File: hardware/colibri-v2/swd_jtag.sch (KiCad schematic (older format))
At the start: 9 parts

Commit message: ADDED R1, R2 R3
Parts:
- added R1, R2, R3: 10K, Resistors_SMD:R_0603, symbol R
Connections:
- net +3V3: now also R1.2, R2.2, R3.2
- net TCK/SWCLK: now also R1.1
- net TDO/SWO: now also R3.1
- net TMS/SWDIO: now also R2.1
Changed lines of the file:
@@
 	1    0    0    -1
 $EndComp
-Wire Wire Line
-	3500 2000 3300 2000
-Wire Wire Line
-	3300 2000 3300 3350
-Wire Wire Line
-	3500 2100 3300 2100
-Connection ~ 3300 2100
-Wire Wire Line
-	3500 2200 3300 2200
-Connection ~ 3300 2200
-Wire Wire Line
-	3500 2300 3300 2300
-Connection ~ 3300 2300
-Wire Wire Line
-	3500 2400 3300 2400
-Connection ~ 3300 2400
-Wire Wire Line
-	3500 2500 3300 2500
-Connection ~ 3300 2500
-Wire Wire Line
-	3500 2600 3300 2600
-Connection ~ 3300 2600
-Wire Wire Line
-	3500 2700 3300 2700
-Connection ~ 3300 2700
-Wire Wire Line
-	3500 2800 3300 2800
-Connection ~ 3300 2800
-Wire Wire Line
-	4000 2000 8500 2000
-Wire Wire Line
-	4000 2100 8500 2100
-Wire Wire Line
-	4000 2200 8500 2200
-Wire Wire Line
-	4000 2300 8500 2300
-Wire Wire Line
-	4000 2500 8500 2500
-Wire Wire Line
-	4000 2600 8500 2600
-Wire Wire Line
-	4000 2800 7650 2800
-Wire Wire Line
-	6700 1700 6700 3050
-Wire Wire Line
-	7300 1700 7300 2000
-Wire Wire Line
-	7000 1700 7000 2100
-Wire Wire Line
-	4000 1900 4050 1900
-Wire Wire Line
-	4050 1900 4050 1200
-Wire Wire Line
-	7300 1200 7300 1400
-Wire Wire Line
-	6700 1200 6700 1400
-Connection ~ 6700 1200
-Connection ~ 7000 1200
-Wire Wire Line
-	3500 1900 3300 1900
-Connection ~ 4050 1200
-Wire Wire Line
-	4000 4600 4950 4600
-Wire Wire Line
-	4000 4700 4950 4700
-Wire Wire Line
-	4000 4900 4950 4900
-Wire Wire Line
-	4150 4500 4000 4500
-Wire Wire Line
-	4150 3900 4150 4500
-Connection ~ 4150 3950
-Wire Wire Line
-	6700 3350 6700 3450
 NoConn ~ 4000 5000
 Text HLabel 8500 2000 2    60   Output ~ 0
@@
 	0    -1   -1   0
 $EndComp
-Wire Wire Line
-	4000 2400 5300 2400
-Wire Wire Line
-	5600 2400 5900 2400
-Wire Wire Line
-	4000 2700 5300 2700
-Wire Wire Line
-	5600 2700 5900 2700
 Text HLabel 8500 2800 2    60   Output ~ 0
 JTAG_POWER_ON
-Wire Wire Line
-	8150 2800 8500 2800
 $Comp
 L +3V3 #PWR?
@@
 	1    0    0    -1
 $EndComp
-Wire Wire Line
-	3300 1200 7300 1200
+Text Label 4950 5100 2    60   ~ 0
+JTAG_POWER
+Text Label 4650 2800 2    60   ~ 0
+JTAG_POWER
+$Comp
+L R R1
+U 1 1 561EC379
+P 7550 1550
+F 0 "R1" V 7600 1750 50  0000 C CNN
+F 1 "10K" V 7557 1551 50  0000 C CNN
+F 2 "Resistors_SMD:R_0603" V 7480 1550 30  0000 C CNN
+F 3 "" H 7550 1550 30  0000 C CNN
+	1    7550 1550
+	-1   0    0    1
+$EndComp
+$Comp
+L R R2
+U 1 1 561EC3BD
+P 7750 1550
+F 0 "R2" V 7800 1750 50  0000 C CNN
+F 1 "10K" V 7757 1551 50  0000 C CNN
+F 2 "Resistors_SMD:R_0603" V 7680 1550 30  0000 C CNN
+F 3 "" H 7750 1550 30  0000 C CNN
+	1    7750 1550
+	-1   0    0    1
+$EndComp
+Wire Wire Line
+	3500 2000 3300 2000
+Wire Wire Line
+	3300 2000 3300 3350
+Wire Wire Line
+	3500 2100 3300 2100
+Connection ~ 3300 2100
+Wire Wire Line
+	3500 2200 3300 2200
+Connection ~ 3300 2200
+Wire Wire Line
+	3500 2300 3300 2300
+Connection ~ 3300 2300
+Wire Wire Line
+	3500 2400 3300 2400
+Connection ~ 3300 2400
+Wire Wire Line
+	3500 2500 3300 2500
+Connection ~ 3300 2500
+Wire Wire Line
+	3500 2600 3300 2600
+Connection ~ 3300 2600
+Wire Wire Line
+	3500 2700 3300 2700
+Connection ~ 3300 2700
+Wire Wire Line
+	3500 2800 3300 2800
+Connection ~ 3300 2800
+Wire Wire Line
+	4000 2000 8500 2000
+Wire Wire Line
+	4000 2100 8500 2100
+Wire Wire Line
+	4000 2200 8500 2200
+Wire Wire Line
+	4000 2300 8500 2300
+Wire Wire Line
+	4000 2500 8500 2500
+Wire Wire Line
+	4000 2600 8500 2600
+Wire Wire Line
+	4000 2800 7650 2800
+Wire Wire Line
+	6700 1700 6700 3050
+Wire Wire Line
+	7300 1700 7300 2000
+Wire Wire Line
+	7000 1700 7000 2100
+Wire Wire Line
+	4000 1900 4050 1900
+Wire Wire Line
+	4050 1900 4050 1200
+Wire Wire Line
+	7300 1200 7300 1400
+Wire Wire Line
+	6700 1200 6700 1400
+Connection ~ 6700 1200
+Connection ~ 7000 1200
+Wire Wire Line
+	3500 1900 3300 1900
+Connection ~ 4050 1200
+Wire Wire Line
+	4000 4600 4950 4600
+Wire Wire Line
+	4000 4700 4950 4700
+Wire Wire Line
+	4000 4900 4950 4900
+Wire Wire Line
+	4150 4500 4000 4500
+Wire Wire Line
+	4150 3900 4150 4500
+Connection ~ 4150 3950
+Wire Wire Line
+	6700 3350 6700 3450
+Wire Wire Line
+	4000 2400 5300 2400
+Wire Wire Line
+	5600 2400 5900 2400
+Wire Wire Line
+	4000 2700 5300 2700
+Wire Wire Line
+	5600 2700 5900 2700
+Wire Wire Line
+	8150 2800 8500 2800
+Wire Wire Line
+	3300 1200 7950 1200
 Connection ~ 6700 2600
 Connection ~ 7000 2100
@@
 Wire Wire Line
 	7000 1400 7000 1200
-Text Label 4950 5100 2    60   ~ 0
-JTAG_POWER
 Wire Wire Line
 	4000 5100 4950 5100
-Text Label 4650 2800 2    60   ~ 0
-JTAG_POWER
 Wire Wire Line
 	4150 5300 4150 4800
 Wire Wire Line
 	4150 4800 4000 4800
+Wire Wire Line
+	7750 1700 7750 2200
+Connection ~ 7750 2200
+Wire Wire Line
+	7550 1700 7550 2300
+Connection ~ 7550 2300
+Wire Wire Line
+	7750 1200 7750 1400
+Connection ~ 7300 1200
+Wire Wire Line
+	7550 1400 7550 1200
+Connection ~ 7550 1200
+$Comp
+L R R3
+U 1 1 561ED2A0
+P 7950 1550
+F 0 "R3" V 8000 1750 50  0000 C CNN
+F 1 "10K" V 7957 1551 50  0000 C CNN
+F 2 "Resistors_SMD:R_0603" V 7880 1550 30  0000 C CNN
+F 3 "" H 7950 1550 30  0000 C CNN
+	1    7950 1550
+	-1   0    0    1
+$EndComp
+Wire Wire Line
+	7950 1700 7950 2500
+Connection ~ 7950 2500
+Wire Wire Line
+	7950 1200 7950 1400
+Connection ~ 7750 1200
 $EndSCHEMATC

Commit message: Annotated Components
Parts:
- gave numbers to parts that had none: 9
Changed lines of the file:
@@
 $EndDescr
 $Comp
-L CONN_02X10 P?
+L CONN_02X10 P1
 U 1 1 55768A13
 P 3750 2350
-F 0 "P?" H 3750 2900 50  0000 C CNN
+F 0 "P1" H 3750 2900 50  0000 C CNN
 F 1 "CONN_02X10" V 3750 2350 50  0000 C CNN
 F 2 "" H 3750 1150 60  0000 C CNN
@@
 $EndComp
 $Comp
-L GND #PWR?
+L GND #PWR11
 U 1 1 55768A1A
 P 3300 3350
-F 0 "#PWR?" H 3300 3100 60  0001 C CNN
+F 0 "#PWR11" H 3300 3100 60  0001 C CNN
 F 1 "GND" H 3300 3200 60  0000 C CNN
 F 2 "" H 3300 3350 60  0000 C CNN
@@
 $EndComp
 $Comp
-L R R?
+L R R15
 U 1 1 55768A2D
 P 5450 2700
-F 0 "R?" V 5500 2900 50  0000 C CNN
+F 0 "R15" V 5500 2900 50  0000 C CNN
 F 1 "10K" V 5457 2701 50  0000 C CNN
 F 2 "Resistors_SMD:R_0603" V 5380 2700 30  0000 C CNN
@@
 $EndComp
 $Comp
-L R R?
+L R R14
 U 1 1 55768A34
 P 5450 2400
-F 0 "R?" V 5500 2600 50  0000 C CNN
+F 0 "R14" V 5500 2600 50  0000 C CNN
 F 1 "10K" V 5457 2401 50  0000 C CNN
 F 2 "Resistors_SMD:R_0603" V 5380 2400 30  0000 C CNN
@@
 $EndComp
 $Comp
-L R R?
+L R R17
 U 1 1 55768A3B
 P 7000 1550
-F 0 "R?" V 7050 1750 50  0000 C CNN
+F 0 "R17" V 7050 1750 50  0000 C CNN
 F 1 "10K" V 7007 1551 50  0000 C CNN
 F 2 "Resistors_SMD:R_0603" V 6930 1550 30  0000 C CNN
@@
 $EndComp
 $Comp
-L R R?
+L R R16
 U 1 1 55768A42
 P 6700 1550
-F 0 "R?" V 6750 1750 50  0000 C CNN
+F 0 "R16" V 6750 1750 50  0000 C CNN
 F 1 "10K" V 6707 1551 50  0000 C CNN
 F 2 "Resistors_SMD:R_0603" V 6630 1550 30  0000 C CNN
@@
 $EndComp
 $Comp
-L R R?
+L R R18
 U 1 1 55768A49
 P 7300 1550
-F 0 "R?" V 7350 1750 50  0000 C CNN
+F 0 "R18" V 7350 1750 50  0000 C CNN
 F 1 "10K" V 7307 1551 50  0000 C CNN
 F 2 "Resistors_SMD:R_0603" V 7230 1550 30  0000 C CNN
@@
 $EndComp
 $Comp
-L CONN_01X07 P?
+L CONN_01X07 P2
 U 1 1 55768A50
 P 3800 4800
-F 0 "P?" H 3800 5200 50  0000 C CNN
+F 0 "P2" H 3800 5200 50  0000 C CNN
 F 1 "CONN_01X07" V 3900 4800 50  0000 C CNN
 F 2 "" H 3800 4800 60  0000 C CNN
@@
 RESET#
 $Comp
-L GND #PWR?
+L GND #PWR13
 U 1 1 55768A5A
 P 4150 5300
-F 0 "#PWR?" H 4150 5050 60  0001 C CNN
+F 0 "#PWR13" H 4150 5050 60  0001 C CNN
 F 1 "GND" H 4150 5150 60  0000 C CNN
 F 2 "" H 4150 5300 60  0000 C CNN
@@
 $EndComp
 $Comp
-L CONN_02X01 P?
+L CONN_02X01 P3
 U 1 1 55768A67
 P 7900 2800
-F 0 "P?" H 7900 2900 50  0000 C CNN
+F 0 "P3" H 7900 2900 50  0000 C CNN
 F 1 "CONN_02X01" H 7900 2700 50  0000 C CNN
 F 2 "" H 7900 1600 60  0000 C CNN
@@
 $EndComp
 $Comp
-L +3V3 #PWR?
+L +3V3 #PWR12
 U 1 1 55768A6E
 P 4150 3900
-F 0 "#PWR?" H 4150 3750 60  0001 C CNN
+F 0 "#PWR12" H 4150 3750 60  0001 C CNN
 F 1 "+3V3" H 4150 4040 60  0000 C CNN
 F 2 "" H 4150 3900 60  0000 C CNN
@@
 $EndComp
 $Comp
-L C C?
+L C C27
 U 1 1 55768A89
 P 6700 3200
-F 0 "C?" H 6750 3300 50  0000 L CNN
+F 0 "C27" H 6750 3300 50  0000 L CNN
 F 1 "100nF/50V" H 6750 3100 50  0000 L CNN
 F 2 "" H 6738 3050 30  0000 C CNN
@@
 $EndComp
 $Comp
-L GND #PWR?
+L GND #PWR17
 U 1 1 55768A90
 P 6700 3450
-F 0 "#PWR?" H 6700 3200 60  0001 C CNN
+F 0 "#PWR17" H 6700 3200 60  0001 C CNN
 F 1 "GND" H 6700 3300 60  0000 C CNN
 F 2 "" H 6700 3450 60  0000 C CNN
@@
 TRST
 $Comp
-L GND #PWR?
+L GND #PWR15
 U 1 1 5576A90F
 P 5900 2400
-F 0 "#PWR?" H 5900 2150 60  0001 C CNN
+F 0 "#PWR15" H 5900 2150 60  0001 C CNN
 F 1 "GND" H 5900 2250 60  0000 C CNN
 F 2 "" H 5900 2400 60  0000 C CNN
@@
 $EndComp
 $Comp
-L GND #PWR?
+L GND #PWR16
 U 1 1 5576A932
 P 5900 2700
-F 0 "#PWR?" H 5900 2450 60  0001 C CNN
+F 0 "#PWR16" H 5900 2450 60  0001 C CNN
 F 1 "GND" H 5900 2550 60  0000 C CNN
 F 2 "" H 5900 2700 60  0000 C CNN
@@
 JTAG_POWER_ON
 $Comp
-L +3V3 #PWR?
+L +3V3 #PWR14
 U 1 1 5576ACC9
 P 5400 1000
-F 0 "#PWR?" H 5400 850 60  0001 C CNN
+F 0 "#PWR14" H 5400 850 60  0001 C CNN
 F 1 "+3V3" H 5400 1140 60  0000 C CNN
 F 2 "" H 5400 1000 60  0000 C CNN

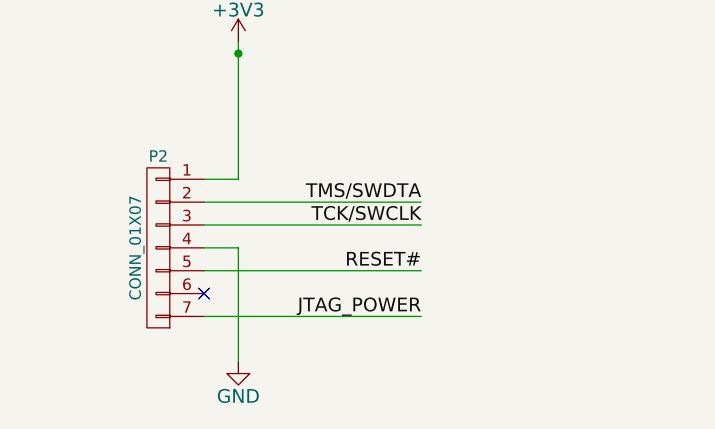
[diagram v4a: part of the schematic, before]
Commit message: Changes in the button sheet
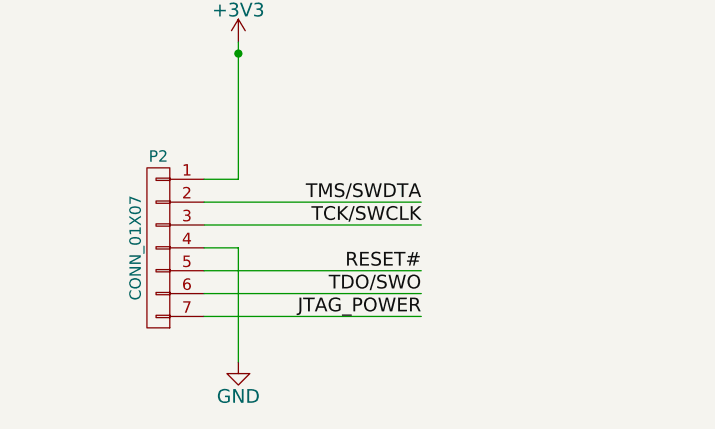
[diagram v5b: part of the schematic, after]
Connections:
- net TDO/SWO: now also P2.6 (P6)
- no-connect marks 1 -> 0
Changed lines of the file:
@@
 	1    0    0    -1
 $EndComp
-NoConn ~ 4000 5000
 Text HLabel 8500 2000 2    60   Output ~ 0
 TRST
@@
 	7950 1200 7950 1400
 Connection ~ 7750 1200
+Text Label 4950 5000 2    60   ~ 0
+TDO/SWO
+Wire Wire Line
+	4000 5000 4950 5000
 $EndSCHEMATC

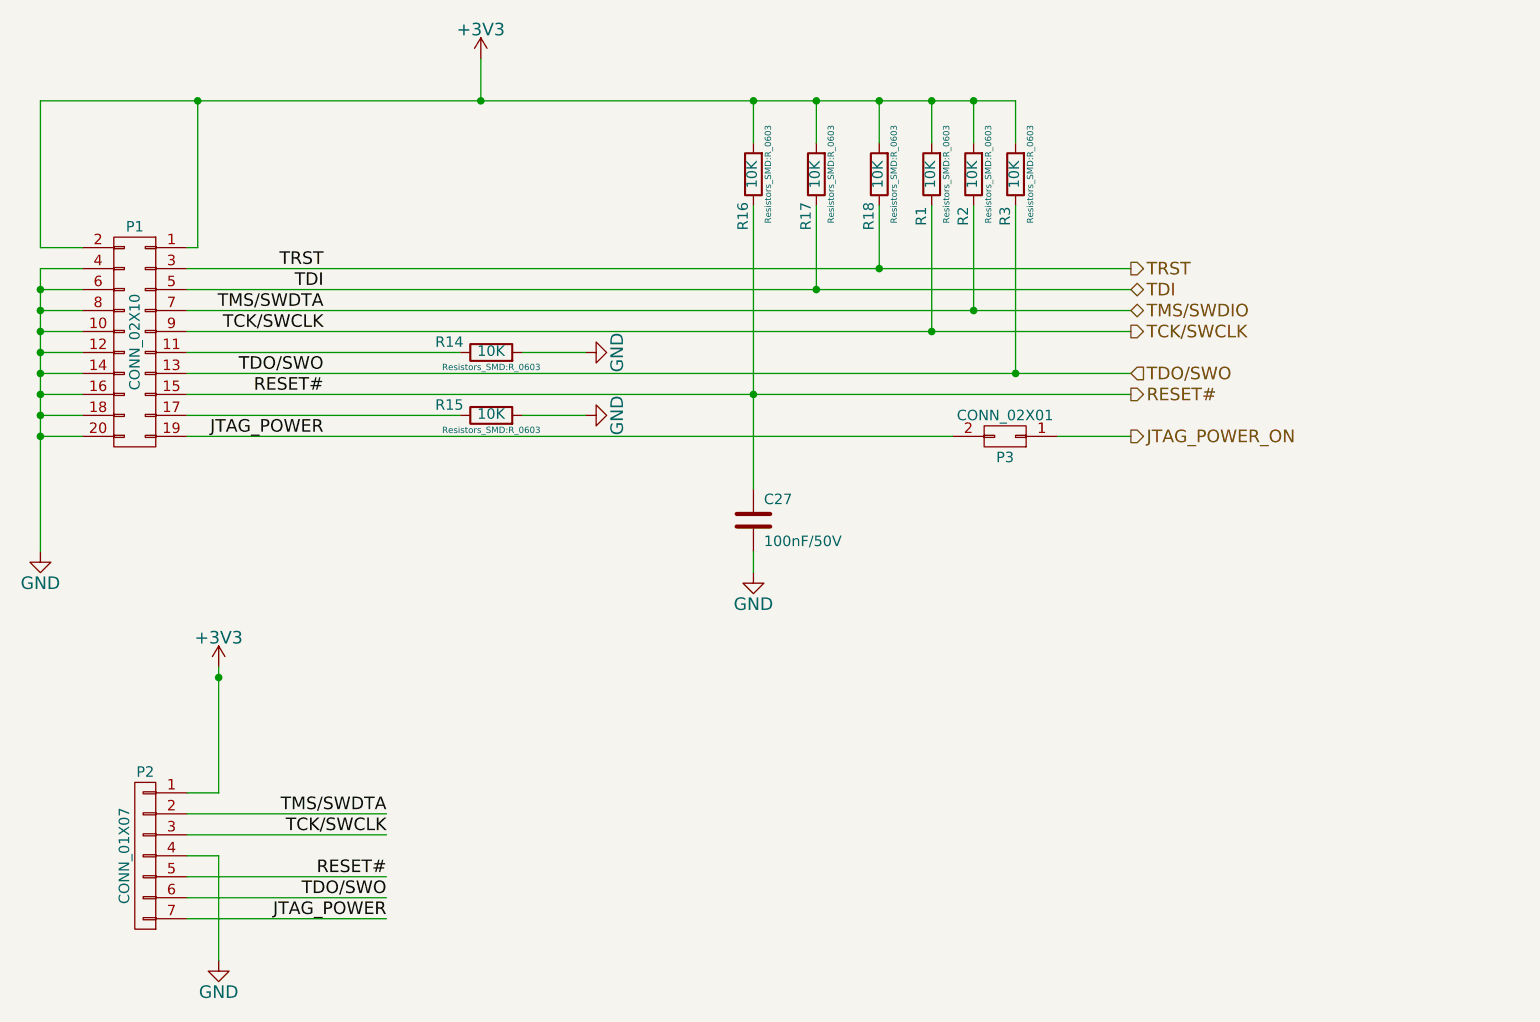
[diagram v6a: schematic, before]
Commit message: Reworked the buttons/leds sheet
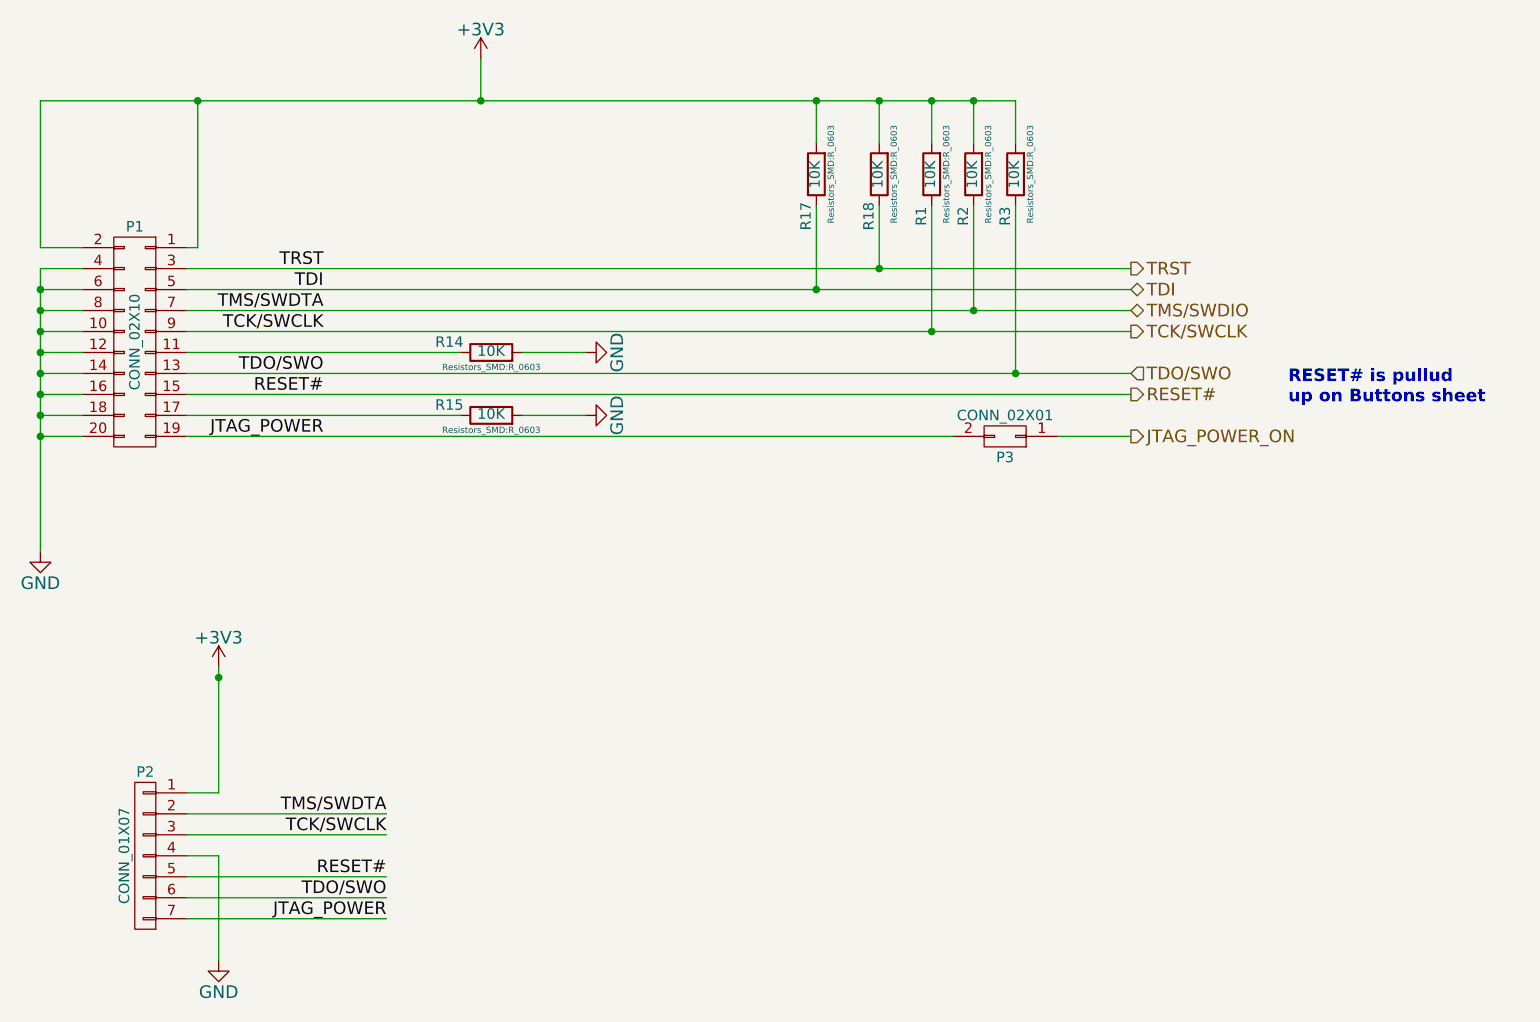
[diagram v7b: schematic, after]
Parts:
- removed C27: 100nF/50V, symbol C
- removed R16: 10K, Resistors_SMD:R_0603, symbol R
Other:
- note added: "RESET# is pullud \nup on Buttons sheet"
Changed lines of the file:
@@
-$EndComp
-$Comp
-L R R16
-U 1 1 55768A42
-P 6700 1550
-F 0 "R16" V 6750 1750 50  0000 C CNN
-F 1 "10K" V 6707 1551 50  0000 C CNN
-F 2 "Resistors_SMD:R_0603" V 6630 1550 30  0000 C CNN
-F 3 "" H 6700 1550 30  0000 C CNN
-	1    6700 1550
-	-1   0    0    1
 $EndComp
 $Comp
@@
 F 3 "" H 4150 3900 60  0000 C CNN
 	1    4150 3900
-	1    0    0    -1
-$EndComp
-$Comp
-L C C27
-U 1 1 55768A89
-P 6700 3200
-F 0 "C27" H 6750 3300 50  0000 L CNN
-F 1 "100nF/50V" H 6750 3100 50  0000 L CNN
-F 2 "" H 6738 3050 30  0000 C CNN
-F 3 "" H 6700 3200 60  0000 C CNN
-	1    6700 3200
-	1    0    0    -1
-$EndComp
-$Comp
-L GND #PWR014
-U 1 1 55768A90
-P 6700 3450
-F 0 "#PWR014" H 6700 3200 60  0001 C CNN
-F 1 "GND" H 6700 3300 60  0000 C CNN
-F 2 "" H 6700 3450 60  0000 C CNN
-F 3 "" H 6700 3450 60  0000 C CNN
-	1    6700 3450
 	1    0    0    -1
 $EndComp
@@
 	4000 2800 7650 2800
 Wire Wire Line
-	6700 1700 6700 3050
-Wire Wire Line
 	7300 1700 7300 2000
 Wire Wire Line
@@
 Wire Wire Line
 	7300 1200 7300 1400
-Wire Wire Line
-	6700 1200 6700 1400
-Connection ~ 6700 1200
 Connection ~ 7000 1200
 Wire Wire Line
@@
 Connection ~ 4150 3950
 Wire Wire Line
-	6700 3350 6700 3450
-Wire Wire Line
 	4000 2400 5300 2400
 Wire Wire Line
@@
 Wire Wire Line
 	3300 1200 7950 1200
-Connection ~ 6700 2600
 Connection ~ 7000 2100
 Connection ~ 7300 2000
@@
 Wire Wire Line
 	4000 5000 4950 5000
+Text Notes 9250 2650 0    60   ~ 12
+RESET# is pullud \nup on Buttons sheet
 $EndSCHEMATC

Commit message: Re-annotated schematic
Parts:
- renumbered R14 to R11, R15 to R12, R17 to R13, R18 to R14, R1 to R15, R2 to R16, R3 to R17
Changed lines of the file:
@@
 $EndComp
 $Comp
-L GND #PWR011
+L GND #PWR11
 U 1 1 55768A1A
 P 3300 3350
-F 0 "#PWR011" H 3300 3100 60  0001 C CNN
+F 0 "#PWR11" H 3300 3100 60  0001 C CNN
 F 1 "GND" H 3300 3200 60  0000 C CNN
 F 2 "" H 3300 3350 60  0000 C CNN
@@
 $EndComp
 $Comp
-L R R15
+L R R12
 U 1 1 55768A2D
 P 5450 2700
-F 0 "R15" V 5500 2900 50  0000 C CNN
+F 0 "R12" V 5500 2900 50  0000 C CNN
 F 1 "10K" V 5457 2701 50  0000 C CNN
-F 2 "Resistors_SMD:R_0603" V 5380 2700 30  0000 C CNN
+F 2 "Resistors_SMD:R_0603" V 5380 2700 30  0001 C CNN
 F 3 "" H 5450 2700 30  0000 C CNN
 	1    5450 2700
@@
 $EndComp
 $Comp
-L R R14
+L R R11
 U 1 1 55768A34
 P 5450 2400
-F 0 "R14" V 5500 2600 50  0000 C CNN
+F 0 "R11" V 5500 2600 50  0000 C CNN
 F 1 "10K" V 5457 2401 50  0000 C CNN
-F 2 "Resistors_SMD:R_0603" V 5380 2400 30  0000 C CNN
+F 2 "Resistors_SMD:R_0603" V 5380 2400 30  0001 C CNN
 F 3 "" H 5450 2400 30  0000 C CNN
 	1    5450 2400
@@
 $EndComp
 $Comp
-L R R17
+L R R13
 U 1 1 55768A3B
 P 7000 1550
-F 0 "R17" V 7050 1750 50  0000 C CNN
+F 0 "R13" V 7050 1750 50  0000 C CNN
 F 1 "10K" V 7007 1551 50  0000 C CNN
-F 2 "Resistors_SMD:R_0603" V 6930 1550 30  0000 C CNN
+F 2 "Resistors_SMD:R_0603" V 6930 1550 30  0001 C CNN
 F 3 "" H 7000 1550 30  0000 C CNN
 	1    7000 1550
@@
 $EndComp
 $Comp
-L R R18
+L R R14
 U 1 1 55768A49
 P 7300 1550
-F 0 "R18" V 7350 1750 50  0000 C CNN
+F 0 "R14" V 7350 1750 50  0000 C CNN
 F 1 "10K" V 7307 1551 50  0000 C CNN
-F 2 "Resistors_SMD:R_0603" V 7230 1550 30  0000 C CNN
+F 2 "Resistors_SMD:R_0603" V 7230 1550 30  0001 C CNN
 F 3 "" H 7300 1550 30  0000 C CNN
 	1    7300 1550
@@
 RESET#
 $Comp
-L GND #PWR012
+L GND #PWR13
 U 1 1 55768A5A
 P 4150 5300
-F 0 "#PWR012" H 4150 5050 60  0001 C CNN
+F 0 "#PWR13" H 4150 5050 60  0001 C CNN
 F 1 "GND" H 4150 5150 60  0000 C CNN
 F 2 "" H 4150 5300 60  0000 C CNN
@@
 $EndComp
 $Comp
-L +3V3 #PWR013
+L +3V3 #PWR12
 U 1 1 55768A6E
 P 4150 3900
-F 0 "#PWR013" H 4150 3750 60  0001 C CNN
+F 0 "#PWR12" H 4150 3750 60  0001 C CNN
 F 1 "+3V3" H 4150 4040 60  0000 C CNN
 F 2 "" H 4150 3900 60  0000 C CNN
@@
 TRST
 $Comp
-L GND #PWR015
+L GND #PWR15
 U 1 1 5576A90F
 P 5900 2400
-F 0 "#PWR015" H 5900 2150 60  0001 C CNN
+F 0 "#PWR15" H 5900 2150 60  0001 C CNN
 F 1 "GND" H 5900 2250 60  0000 C CNN
 F 2 "" H 5900 2400 60  0000 C CNN
@@
 $EndComp
 $Comp
-L GND #PWR016
+L GND #PWR16
 U 1 1 5576A932
 P 5900 2700
-F 0 "#PWR016" H 5900 2450 60  0001 C CNN
+F 0 "#PWR16" H 5900 2450 60  0001 C CNN
 F 1 "GND" H 5900 2550 60  0000 C CNN
 F 2 "" H 5900 2700 60  0000 C CNN
@@
 JTAG_POWER_ON
 $Comp
-L +3V3 #PWR017
+L +3V3 #PWR14
 U 1 1 5576ACC9
 P 5400 1000
-F 0 "#PWR017" H 5400 850 60  0001 C CNN
+F 0 "#PWR14" H 5400 850 60  0001 C CNN
 F 1 "+3V3" H 5400 1140 60  0000 C CNN
 F 2 "" H 5400 1000 60  0000 C CNN
@@
 JTAG_POWER
 $Comp
-L R R1
+L R R15
 U 1 1 561EC379
 P 7550 1550
-F 0 "R1" V 7600 1750 50  0000 C CNN
+F 0 "R15" V 7600 1750 50  0000 C CNN
 F 1 "10K" V 7557 1551 50  0000 C CNN
-F 2 "Resistors_SMD:R_0603" V 7480 1550 30  0000 C CNN
+F 2 "Resistors_SMD:R_0603" V 7480 1550 30  0001 C CNN
 F 3 "" H 7550 1550 30  0000 C CNN
 	1    7550 1550
@@
 $EndComp
 $Comp
-L R R2
+L R R16
 U 1 1 561EC3BD
 P 7750 1550
-F 0 "R2" V 7800 1750 50  0000 C CNN
+F 0 "R16" V 7800 1750 50  0000 C CNN
 F 1 "10K" V 7757 1551 50  0000 C CNN
-F 2 "Resistors_SMD:R_0603" V 7680 1550 30  0000 C CNN
+F 2 "Resistors_SMD:R_0603" V 7680 1550 30  0001 C CNN
 F 3 "" H 7750 1550 30  0000 C CNN
 	1    7750 1550
@@
 Connection ~ 7550 1200
 $Comp
-L R R3
+L R R17
 U 1 1 561ED2A0
 P 7950 1550
-F 0 "R3" V 8000 1750 50  0000 C CNN
+F 0 "R17" V 8000 1750 50  0000 C CNN
 F 1 "10K" V 7957 1551 50  0000 C CNN
-F 2 "Resistors_SMD:R_0603" V 7880 1550 30  0000 C CNN
+F 2 "Resistors_SMD:R_0603" V 7880 1550 30  0001 C CNN
 F 3 "" H 7950 1550 30  0000 C CNN
 	1    7950 1550
